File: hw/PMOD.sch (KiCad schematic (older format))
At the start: 1 part, among them J4 Conn_02x06_Odd_Even

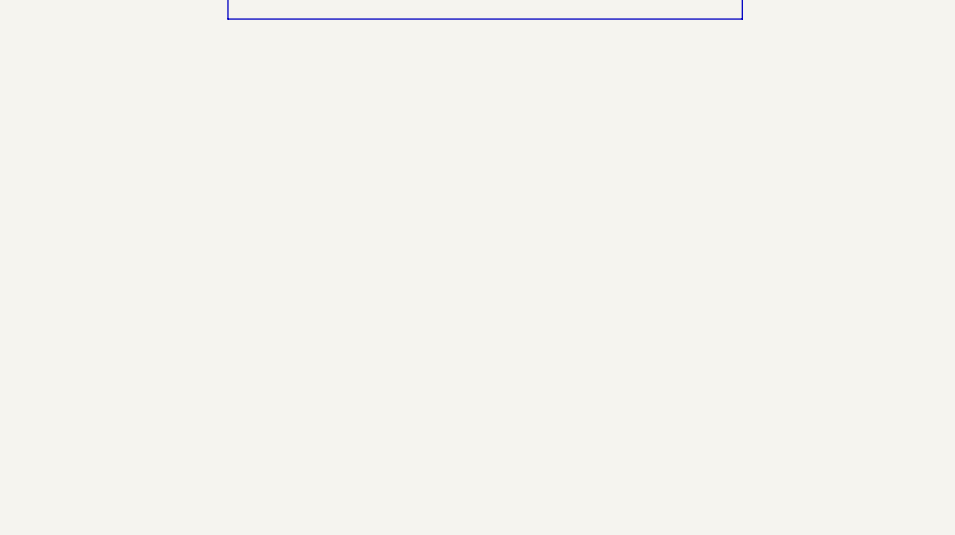
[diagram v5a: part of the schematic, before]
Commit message: Add ESD protection
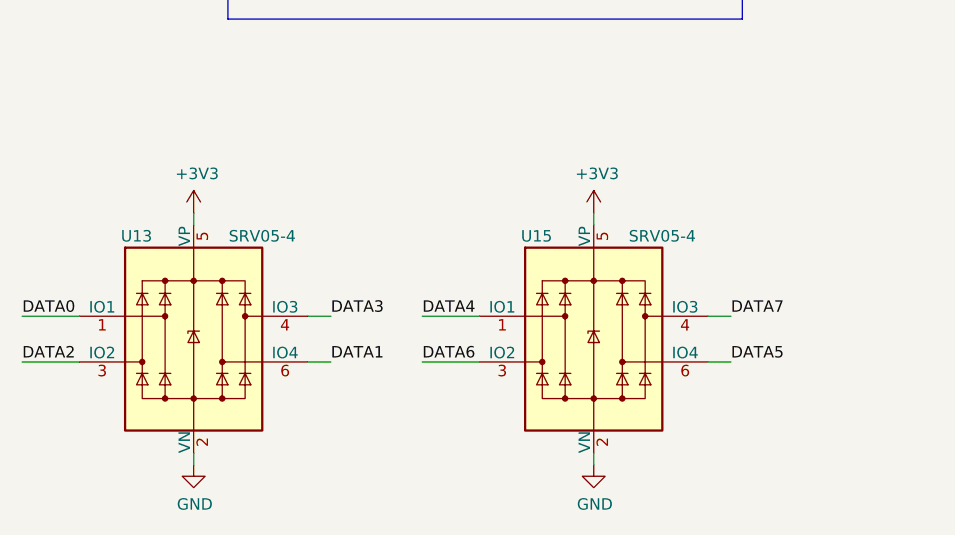
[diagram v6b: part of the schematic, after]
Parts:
- added U12, U14: SRV05-4, Package_TO_SOT_SMD:SOT-23-6, symbol Power_Protection:SRV05-4
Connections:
- net +3V3: now also U12.5 (VP), U14.5 (VP)
- net DATA0: now also U12.1 (IO1)
- net DATA1: now also U12.6 (IO4)
- net DATA2: now also U12.3 (IO2)
- net DATA3: now also U12.4 (IO3)
- net DATA4: now also U14.1 (IO1)
- net DATA5: now also U14.6 (IO4)
- net DATA6: now also U14.3 (IO2)
- net DATA7: now also U14.4 (IO3)
- net GND: now also U12.2 (VN), U14.2 (VN)
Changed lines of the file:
@@
 $Descr A4 11693 8268
 encoding utf-8
-Sheet 6 11
+Sheet 7 11
 Title ""
 Date ""
@@
 U 1 1 5EA5FB48
 P 6050 4050
-AR Path="/5EA5DA36/5EA5FB48" Ref="#PWR0102" Part="1"
-AR Path="/5EA6C61B/5EA5FB48" Ref="#PWR0106" Part="1"
-F 0 "#PWR0106" H 6050 3800 50 0001 C CNN
-F 1 "GND" H 6055 3877 50 0000 C CNN
-F 2 "" H 6050 4050 50 0001 C CNN
-F 3 "" H 6050 4050 50 0001 C CNN
+AR Path="/5EA5DA36/5EA5FB48" Ref="#PWR0102"  Part="1"
+AR Path="/5EA6C61B/5EA5FB48" Ref="#PWR0106"  Part="1"
+F 0 "#PWR0106" H 6050 3800 50  0001 C CNN
+F 1 "GND" H 6055 3877 50  0000 C CNN
+F 2 "" H 6050 4050 50  0001 C CNN
+F 3 "" H 6050 4050 50  0001 C CNN
 	1    6050 4050
 	1    0    0    -1
@@
 U 1 1 5EA6052D
 P 5450 4050
-AR Path="/5EA5DA36/5EA6052D" Ref="#PWR0101" Part="1"
-AR Path="/5EA6C61B/5EA6052D" Ref="#PWR0105" Part="1"
-F 0 "#PWR0105" H 5450 3800 50 0001 C CNN
-F 1 "GND" H 5455 3877 50 0000 C CNN
-F 2 "" H 5450 4050 50 0001 C CNN
-F 3 "" H 5450 4050 50 0001 C CNN
+AR Path="/5EA5DA36/5EA6052D" Ref="#PWR0101"  Part="1"
+AR Path="/5EA6C61B/5EA6052D" Ref="#PWR0105"  Part="1"
+F 0 "#PWR0105" H 5450 3800 50  0001 C CNN
+F 1 "GND" H 5455 3877 50  0000 C CNN
+F 2 "" H 5450 4050 50  0001 C CNN
+F 3 "" H 5450 4050 50  0001 C CNN
 	1    5450 4050
 	1    0    0    -1
@@
 U 1 1 5EA60E2D
 P 6050 3300
-AR Path="/5EA5DA36/5EA60E2D" Ref="#PWR0103" Part="1"
-AR Path="/5EA6C61B/5EA60E2D" Ref="#PWR0107" Part="1"
-F 0 "#PWR0107" H 6050 3150 50 0001 C CNN
-F 1 "+3V3" H 6065 3473 50 0000 C CNN
-F 2 "" H 6050 3300 50 0001 C CNN
-F 3 "" H 6050 3300 50 0001 C CNN
+AR Path="/5EA5DA36/5EA60E2D" Ref="#PWR0103"  Part="1"
+AR Path="/5EA6C61B/5EA60E2D" Ref="#PWR0107"  Part="1"
+F 0 "#PWR0107" H 6050 3150 50  0001 C CNN
+F 1 "+3V3" H 6065 3473 50  0000 C CNN
+F 2 "" H 6050 3300 50  0001 C CNN
+F 3 "" H 6050 3300 50  0001 C CNN
 	1    6050 3300
 	1    0    0    -1
@@
 U 1 1 5EA61156
 P 5450 3300
-AR Path="/5EA5DA36/5EA61156" Ref="#PWR0100" Part="1"
-AR Path="/5EA6C61B/5EA61156" Ref="#PWR0104" Part="1"
-F 0 "#PWR0104" H 5450 3150 50 0001 C CNN
-F 1 "+3V3" H 5465 3473 50 0000 C CNN
-F 2 "" H 5450 3300 50 0001 C CNN
-F 3 "" H 5450 3300 50 0001 C CNN
+AR Path="/5EA5DA36/5EA61156" Ref="#PWR0100"  Part="1"
+AR Path="/5EA6C61B/5EA61156" Ref="#PWR0104"  Part="1"
+F 0 "#PWR0104" H 5450 3150 50  0001 C CNN
+F 1 "+3V3" H 5465 3473 50  0000 C CNN
+F 2 "" H 5450 3300 50  0001 C CNN
+F 3 "" H 5450 3300 50  0001 C CNN
 	1    5450 3300
 	1    0    0    -1
@@
 U 1 1 5DB0E5EC
 P 5700 3650
-AR Path="/5EA5DA36/5DB0E5EC" Ref="J4" Part="1"
-AR Path="/5EA6C61B/5DB0E5EC" Ref="J5" Part="1"
-F 0 "J5" H 5750 3950 50 0000 C CNN
-F 1 "Conn_02x06_Odd_Even" H 5700 4400 50 0000 C CNN
-F 2 "Connector_PinSocket_2.54mm:PinSocket_2x06_P2.54mm_Horizontal" H 5700 3650 50 0001 C CNN
-F 3 "~" H 5700 3650 50 0001 C CNN
-F 4 "0" H 5750 4050 50 0001 C CNN "JLCPCB BOM"
+AR Path="/5EA5DA36/5DB0E5EC" Ref="J4"  Part="1"
+AR Path="/5EA6C61B/5DB0E5EC" Ref="J5"  Part="1"
+F 0 "J5" H 5750 3950 50  0000 C CNN
+F 1 "Conn_02x06_Odd_Even" H 5700 4400 50  0000 C CNN
+F 2 "Connector_PinSocket_2.54mm:PinSocket_2x06_P2.54mm_Horizontal" H 5700 3650 50  0001 C CNN
+F 3 "~" H 5700 3650 50  0001 C CNN
+F 4 "0" H 5750 4050 50  0001 C CNN "JLCPCB BOM"
 	1    5700 3650
 	1    0    0    -1
@@
 Wire Wire Line
 	6050 3450 6000 3450
+Entry Wire Line
+	4650 3550 4750 3650
+Entry Wire Line
+	4650 3650 4750 3750
+Entry Wire Line
+	4650 3750 4750 3850
+Entry Wire Line
+	4650 3850 4750 3950
+Entry Wire Line
+	6900 3550 6800 3650
+Entry Wire Line
+	6900 3650 6800 3750
+Entry Wire Line
+	6900 3750 6800 3850
+Entry Wire Line
+	6900 3850 6800 3950
+$Comp
+L power:GND #PWR?
+U 1 1 5DD2B31C
+P 4500 6350
+AR Path="/5DD2B31C" Ref="#PWR?"  Part="1"
+AR Path="/5EA5DA36/5DD2B31C" Ref="#PWR0153"  Part="1"
+AR Path="/5EA6C61B/5DD2B31C" Ref="#PWR0155"  Part="1"
+F 0 "#PWR0155" H 4500 6100 50  0001 C CNN
+F 1 "GND" H 4505 6177 50  0000 C CNN
+F 2 "" H 4500 6350 50  0001 C CNN
+F 3 "" H 4500 6350 50  0001 C CNN
+	1    4500 6350
+	1    0    0    -1
+$EndComp
+Wire Wire Line
+	4500 6300 4500 6350
+$Comp
+L Power_Protection:SRV05-4 U?
+U 1 1 5DD2B329
+P 4500 5800
+AR Path="/5DD2B329" Ref="U?"  Part="1"
+AR Path="/5EA5DA36/5DD2B329" Ref="U12"  Part="1"
+AR Path="/5EA6C61B/5DD2B329" Ref="U13"  Part="1"
+F 0 "U13" H 4250 6250 50  0000 C CNN
+F 1 "SRV05-4" H 4800 6250 50  0000 C CNN
+F 2 "Package_TO_SOT_SMD:SOT-23-6" H 5200 5350 50  0001 C CNN
+F 3 "~" H 4500 5800 50  0001 C CNN
+F 4 "C85364" H 4500 5800 50  0001 C CNN "LCSC Part"
+	1    4500 5800
+	1    0    0    -1
+$EndComp
+Wire Wire Line
+	3750 5700 4000 5700
+Wire Wire Line
+	4000 5900 3750 5900
+Wire Wire Line
+	5000 5700 5100 5700
+Wire Wire Line
+	5000 5900 5100 5900
+Text Label 3750 5700 0    50   ~ 0
+DATA0
+Text Label 3750 5900 0    50   ~ 0
+DATA2
+Text Label 5100 5700 0    50   ~ 0
+DATA3
+Text Label 5100 5900 0    50   ~ 0
+DATA1
+$Comp
+L power:+3V3 #PWR0152
+U 1 1 5DD2F395
+P 4500 5250
+AR Path="/5EA5DA36/5DD2F395" Ref="#PWR0152"  Part="1"
+AR Path="/5EA6C61B/5DD2F395" Ref="#PWR0154"  Part="1"
+F 0 "#PWR0154" H 4500 5100 50  0001 C CNN
+F 1 "+3V3" H 4515 5423 50  0000 C CNN
+F 2 "" H 4500 5250 50  0001 C CNN
+F 3 "" H 4500 5250 50  0001 C CNN
+	1    4500 5250
+	1    0    0    -1
+$EndComp
+Wire Wire Line
+	4500 5250 4500 5300
+$Comp
+L power:GND #PWR?
+U 1 1 5DD3395B
+P 6250 6350
+AR Path="/5DD3395B" Ref="#PWR?"  Part="1"
+AR Path="/5EA5DA36/5DD3395B" Ref="#PWR0157"  Part="1"
+AR Path="/5EA6C61B/5DD3395B" Ref="#PWR0159"  Part="1"
+F 0 "#PWR0159" H 6250 6100 50  0001 C CNN
+F 1 "GND" H 6255 6177 50  0000 C CNN
+F 2 "" H 6250 6350 50  0001 C CNN
+F 3 "" H 6250 6350 50  0001 C CNN
+	1    6250 6350
+	1    0    0    -1
+$EndComp
+Wire Wire Line
+	6250 6300 6250 6350
+$Comp
+L Power_Protection:SRV05-4 U?
+U 1 1 5DD33963
+P 6250 5800
+AR Path="/5DD33963" Ref="U?"  Part="1"
+AR Path="/5EA5DA36/5DD33963" Ref="U14"  Part="1"
+AR Path="/5EA6C61B/5DD33963" Ref="U15"  Part="1"
+F 0 "U15" H 6000 6250 50  0000 C CNN
+F 1 "SRV05-4" H 6550 6250 50  0000 C CNN
+F 2 "Package_TO_SOT_SMD:SOT-23-6" H 6950 5350 50  0001 C CNN
+F 3 "~" H 6250 5800 50  0001 C CNN
+F 4 "C85364" H 6250 5800 50  0001 C CNN "LCSC Part"
+	1    6250 5800
+	1    0    0    -1
+$EndComp
+Wire Wire Line
+	5500 5700 5750 5700
+Wire Wire Line
+	5750 5900 5500 5900
+Wire Wire Line
+	6750 5700 6850 5700
+Wire Wire Line
+	6750 5900 6850 5900
+Text Label 5500 5700 0    50   ~ 0
+DATA4
+Text Label 5500 5900 0    50   ~ 0
+DATA6
+Text Label 6850 5700 0    50   ~ 0
+DATA7
+Text Label 6850 5900 0    50   ~ 0
+DATA5
+$Comp
+L power:+3V3 #PWR0156
+U 1 1 5DD33971
+P 6250 5250
+AR Path="/5EA5DA36/5DD33971" Ref="#PWR0156"  Part="1"
+AR Path="/5EA6C61B/5DD33971" Ref="#PWR0158"  Part="1"
+F 0 "#PWR0158" H 6250 5100 50  0001 C CNN
+F 1 "+3V3" H 6265 5423 50  0000 C CNN
+F 2 "" H 6250 5250 50  0001 C CNN
+F 3 "" H 6250 5250 50  0001 C CNN
+	1    6250 5250
+	1    0    0    -1
+$EndComp
+Wire Wire Line
+	6250 5250 6250 5300
 Wire Bus Line
 	6900 3350 6900 4400
 Wire Bus Line
 	4650 3300 4650 4400
-Entry Wire Line
-	4650 3550 4750 3650
-Entry Wire Line
-	4650 3650 4750 3750
-Entry Wire Line
-	4650 3750 4750 3850
-Entry Wire Line
-	4650 3850 4750 3950
-Entry Wire Line
-	6900 3550 6800 3650
-Entry Wire Line
-	6900 3650 6800 3750
-Entry Wire Line
-	6900 3750 6800 3850
-Entry Wire Line
-	6900 3850 6800 3950
 $EndSCHEMATC

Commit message: Fix JLC rotation
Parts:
- U12, U14: JLCPCB Rotation (none) -> 180
